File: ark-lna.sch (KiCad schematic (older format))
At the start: 16 parts, among them P1 CONN_1, P2 CONN_1, U1 LM1117-5, U2 MAR-6+

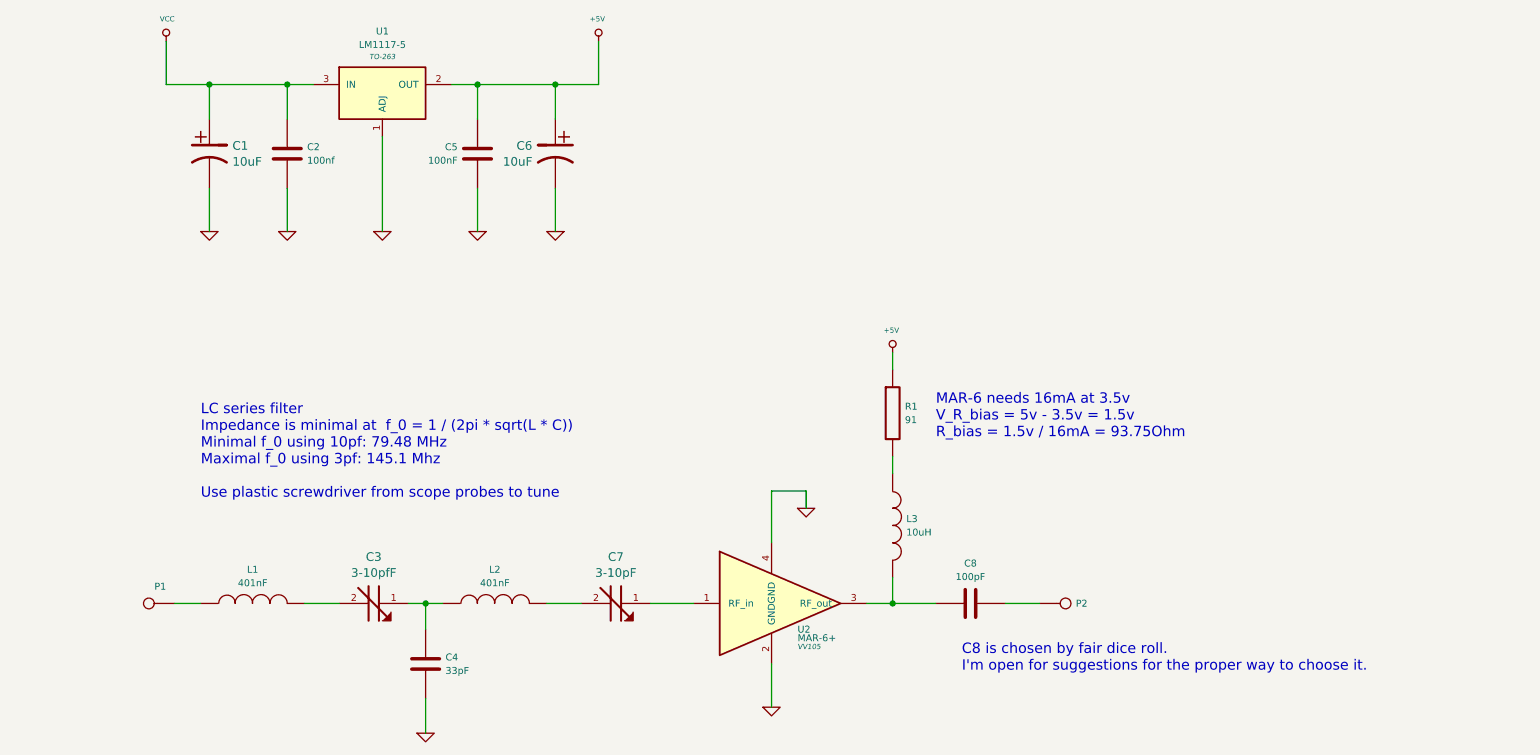
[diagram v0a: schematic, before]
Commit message: Exchanged inductors for better availability Started layouting
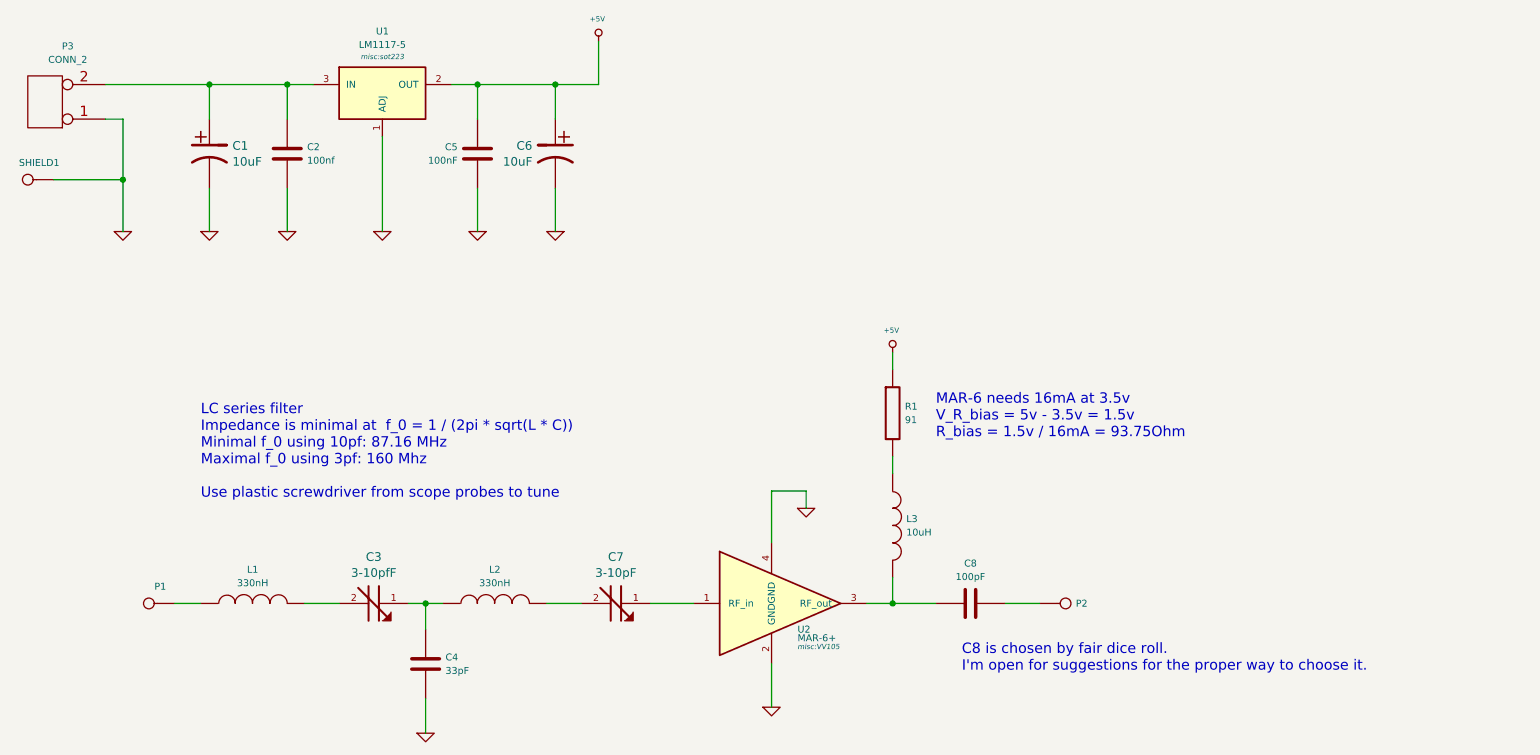
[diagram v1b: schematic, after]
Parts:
- added P3: CONN_2, connect:SIL-2, symbol CONN_2
- added SHIELD1: CONN_1, misc:teko371, symbol CONN_1
- C1, C6: footprint (none) -> smd_capacitors:c_elec_4x5.3
- C2, C5, R1: footprint (none) -> libcms:SM0603
- C3, C7: footprint (none) -> misc:TZC3
- C4, C8, L3: footprint (none) -> libcms:SM0805
- L1, L2: value 401nF -> 330nH; footprint (none) -> libcms:SM0805
- P1, P2: footprint (none) -> connect:1pin
- U1: footprint TO-263 -> misc:sot223
- U2: footprint VV105 -> misc:VV105
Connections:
- net GND: now also P3.1 (P1), SHIELD1.1
- net VCC: no longer names the net of C1.1, C2.1, U1.3 (IN)
- net VCC: now also P3.2 (PM)
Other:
- note added: "LC series filter\nImpedance is minimal at f_0 = 1 / (2pi * sqrt(L * C))\nMinimal f_0 using 10pf: 87.16 MHz\nMaximal f_0 using 3pf: 160 Mhz\n\nUse plastic screwdriver from scope probes to tune"
- note removed: "LC series filter\nImpedance is minimal at f_0 = 1 / (2pi * sqrt(L * C))\nMinimal f_0 using 10pf: 79.48 MHz\nMaximal f_0 using 3pf: 145.1 Mhz\n\nUse plastic screwdriver from scope probes to tune"
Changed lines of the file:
@@
 LIBS:valves
 LIBS:mar-6
+LIBS:ark-lna-cache
 EELAYER 25 0
 EELAYER END
@@
 encoding utf-8
 Sheet 1 1
-Title ""
-Date ""
-Rev ""
-Comp ""
+Title "Ark-LNA"
+Date "2016-06-09"
+Rev "0.1"
+Comp "Abteilung für Angewandte Raumfahrt - Chaos inKL."
 Comment1 ""
 Comment2 ""
@@
 F 0 "P1" H 2984 4452 40  0000 C CNN
 F 1 "CONN_1" H 3050 4605 30  0001 C CNN
-F 2 "" H 3050 4550 60  0000 C CNN
+F 2 "connect:1pin" H 3050 4550 60  0001 C CNN
 F 3 "" H 3050 4550 60  0000 C CNN
 	1    3050 4550
@@
 P 3650 4550
 F 0 "L1" V 3846 4550 40  0000 C CNN
-F 1 "401nF" V 3768 4550 40  0000 C CNN
-F 2 "" H 3650 4550 60  0000 C CNN
+F 1 "330nH" V 3768 4550 40  0000 C CNN
+F 2 "libcms:SM0805" H 3650 4550 60  0001 C CNN
 F 3 "" H 3650 4550 60  0000 C CNN
 	1    3650 4550
@@
 P 5050 4550
 F 0 "L2" V 5246 4550 40  0000 C CNN
-F 1 "401nF" V 5168 4550 40  0000 C CNN
-F 2 "" H 5050 4550 60  0000 C CNN
+F 1 "330nH" V 5168 4550 40  0000 C CNN
+F 2 "libcms:SM0805" H 5050 4550 60  0001 C CNN
 F 3 "" H 5050 4550 60  0000 C CNN
 	1    5050 4550
@@
 F 0 "C3" V 4081 4550 50  0000 C CNN
 F 1 "3-10pfF" V 4173 4550 50  0000 C CNN
-F 2 "" H 4350 4550 60  0000 C CNN
+F 2 "misc:TZC3" H 4350 4550 60  0001 C CNN
 F 3 "" H 4350 4550 60  0000 C CNN
 	1    4350 4550
@@
 F 0 "C7" V 5481 4550 50  0000 C CNN
 F 1 "3-10pF" V 5573 4550 50  0000 C CNN
-F 2 "" H 5750 4550 60  0000 C CNN
+F 2 "misc:TZC3" H 5750 4550 60  0001 C CNN
 F 3 "" H 5750 4550 60  0000 C CNN
 	1    5750 4550
@@
 F 0 "C4" H 4765 4939 40  0000 L CNN
 F 1 "33pF" H 4765 4861 40  0000 L CNN
-F 2 "" H 4688 4750 30  0000 C CNN
+F 2 "libcms:SM0805" H 4688 4750 30  0001 C CNN
 F 3 "" H 4650 4900 60  0000 C CNN
 	1    4650 4900
@@
 	4650 5100 4650 5300
 $Comp
-L GND #PWR5
+L GND #PWR01
 U 1 1 5755E6CD
 P 4650 5300
-F 0 "#PWR5" H 4650 5300 30  0001 C CNN
+F 0 "#PWR01" H 4650 5300 30  0001 C CNN
 F 1 "GND" H 4650 5230 30  0001 C CNN
 F 2 "" H 4650 5300 60  0000 C CNN
@@
 F 0 "U2" H 6800 4400 40  0000 L CNN
 F 1 "MAR-6+" H 6800 4350 40  0000 L CNN
-F 2 "VV105" H 6800 4300 30  0000 L CIN
+F 2 "misc:VV105" H 6800 4300 30  0000 L CIN
 F 3 "" H 6650 4550 60  0000 C CNN
 	1    6650 4550
@@
 	6650 4900 6650 5150
 $Comp
-L GND #PWR10
+L GND #PWR02
 U 1 1 5755E929
 P 6850 4000
-F 0 "#PWR10" H 6850 4000 30  0001 C CNN
+F 0 "#PWR02" H 6850 4000 30  0001 C CNN
 F 1 "GND" H 6850 3930 30  0001 C CNN
 F 2 "" H 6850 4000 60  0000 C CNN
@@
 $EndComp
 $Comp
-L GND #PWR9
+L GND #PWR03
 U 1 1 5755E97C
 P 6650 5150
-F 0 "#PWR9" H 6650 5150 30  0001 C CNN
+F 0 "#PWR03" H 6650 5150 30  0001 C CNN
 F 1 "GND" H 6650 5080 30  0001 C CNN
 F 2 "" H 6650 5150 60  0000 C CNN
@@
 F 0 "L3" H 7429 4139 40  0000 L CNN
 F 1 "10uH" H 7429 4061 40  0000 L CNN
-F 2 "" H 7350 4100 60  0000 C CNN
+F 2 "libcms:SM0805" H 7350 4100 60  0001 C CNN
 F 3 "" H 7350 4100 60  0000 C CNN
 	1    7350 4100
@@
 F 0 "R1" H 7421 3489 40  0000 L CNN
 F 1 "91" H 7421 3411 40  0000 L CNN
-F 2 "" V 7280 3450 30  0000 C CNN
+F 2 "libcms:SM0603" V 7280 3450 30  0001 C CNN
 F 3 "" H 7350 3450 30  0000 C CNN
 	1    7350 3450
@@
 F 0 "P2" H 8409 4550 40  0000 L CNN
 F 1 "CONN_1" H 8350 4605 30  0001 C CNN
-F 2 "" H 8350 4550 60  0000 C CNN
+F 2 "connect:1pin" H 8350 4550 60  0001 C CNN
 F 3 "" H 8350 4550 60  0000 C CNN
 	1    8350 4550
@@
 $EndComp
 $Comp
-L +5V #PWR11
+L +5V #PWR04
 U 1 1 5755ED66
 P 7350 3100
-F 0 "#PWR11" H 7350 3190 20  0001 C CNN
+F 0 "#PWR04" H 7350 3190 20  0001 C CNN
 F 1 "+5V" H 7343 3229 30  0000 C CNN
 F 2 "" H 7350 3100 60  0000 C CNN
@@
 F 0 "C8" V 7568 4550 40  0000 C CNN
 F 1 "100pF" V 7646 4550 40  0000 C CNN
-F 2 "" H 7838 4400 30  0000 C CNN
+F 2 "libcms:SM0805" H 7838 4400 30  0001 C CNN
 F 3 "" H 7800 4550 60  0000 C CNN
 	1    7800 4550
@@
 	8000 4550 8200 4550
 Text Notes 3350 3950 0    60   ~ 0
-LC series filter\nImpedance is minimal at  f_0 = 1 / (2pi * sqrt(L * C))\nMinimal f_0 using 10pf: 79.48 MHz\nMaximal f_0 using 3pf: 145.1 Mhz\n\nUse plastic screwdriver from scope probes to tune
+LC series filter\nImpedance is minimal at  f_0 = 1 / (2pi * sqrt(L * C))\nMinimal f_0 using 10pf: 87.16 MHz\nMaximal f_0 using 3pf: 160 Mhz\n\nUse plastic screwdriver from scope probes to tune
 $Comp
 L LM317S U1
@@
 F 0 "U1" H 4400 1958 40  0000 C CNN
 F 1 "LM1117-5" H 4400 1880 40  0000 C CNN
-F 2 "TO-263" H 4400 1811 30  0000 C CIN
+F 2 "misc:sot223" H 4400 1811 30  0000 C CIN
 F 3 "" H 4400 1600 60  0000 C CNN
 	1    4400 1600
@@
 $EndComp
 $Comp
-L GND #PWR4
+L GND #PWR05
 U 1 1 57560406
 P 4400 2400
-F 0 "#PWR4" H 4400 2400 30  0001 C CNN
+F 0 "#PWR05" H 4400 2400 30  0001 C CNN
 F 1 "GND" H 4400 2330 30  0001 C CNN
 F 2 "" H 4400 2400 60  0000 C CNN
@@
 	1    0    0    -1
 $EndComp
-$Comp
-L VCC #PWR1
-U 1 1 57560432
-P 3150 1300
-F 0 "#PWR1" H 3150 1400 30  0001 C CNN
-F 1 "VCC" H 3156 1429 30  0000 C CNN
-F 2 "" H 3150 1300 60  0000 C CNN
-F 3 "" H 3150 1300 60  0000 C CNN
-	1    3150 1300
-	1    0    0    -1
-$EndComp
-Wire Wire Line
-	3150 1300 3150 1550
-Wire Wire Line
-	3150 1550 4000 1550
+Wire Wire Line
+	2800 1550 4000 1550
 $Comp
 L CP1 C1
@@
 F 0 "C1" H 3533 1996 50  0000 L CNN
 F 1 "10uF" H 3533 1904 50  0000 L CNN
-F 2 "" H 3400 1950 60  0000 C CNN
+F 2 "smd_capacitors:c_elec_4x5.3" H 3400 1950 60  0001 C CNN
 F 3 "" H 3400 1950 60  0000 C CNN
 	1    3400 1950
@@
 F 0 "C2" H 3965 1989 40  0000 L CNN
 F 1 "100nf" H 3965 1911 40  0000 L CNN
-F 2 "" H 3965 1872 30  0000 L CNN
+F 2 "libcms:SM0603" H 3965 1872 30  0001 L CNN
 F 3 "" H 3850 1950 60  0000 C CNN
 	1    3850 1950
@@
 	4400 2400 4400 1850
 $Comp
-L GND #PWR3
+L GND #PWR06
 U 1 1 57560722
 P 3850 2400
-F 0 "#PWR3" H 3850 2400 30  0001 C CNN
+F 0 "#PWR06" H 3850 2400 30  0001 C CNN
 F 1 "GND" H 3850 2330 30  0001 C CNN
 F 2 "" H 3850 2400 60  0000 C CNN
@@
 $EndComp
 $Comp
-L GND #PWR2
+L GND #PWR07
 U 1 1 57560752
 P 3400 2400
-F 0 "#PWR2" H 3400 2400 30  0001 C CNN
+F 0 "#PWR07" H 3400 2400 30  0001 C CNN
 F 1 "GND" H 3400 2330 30  0001 C CNN
 F 2 "" H 3400 2400 60  0000 C CNN
@@
 F 0 "C6" H 5533 1996 50  0000 L CNN
 F 1 "10uF" H 5533 1904 50  0000 L CNN
-F 2 "" H 5400 1950 60  0000 C CNN
+F 2 "smd_capacitors:c_elec_4x5.3" H 5400 1950 60  0001 C CNN
 F 3 "" H 5400 1950 60  0000 C CNN
 	1    5400 1950
@@
 F 0 "C5" H 5065 1989 40  0000 L CNN
 F 1 "100nF" H 5065 1911 40  0000 L CNN
-F 2 "" H 4988 1800 30  0000 C CNN
+F 2 "libcms:SM0603" H 4988 1800 30  0001 C CNN
 F 3 "" H 4950 1950 60  0000 C CNN
 	1    4950 1950
@@
 	4950 2400 4950 2150
 $Comp
-L GND #PWR6
+L GND #PWR08
 U 1 1 57560990
 P 4950 2400
-F 0 "#PWR6" H 4950 2400 30  0001 C CNN
+F 0 "#PWR08" H 4950 2400 30  0001 C CNN
 F 1 "GND" H 4950 2330 30  0001 C CNN
 F 2 "" H 4950 2400 60  0000 C CNN
@@
 $EndComp
 $Comp
-L GND #PWR7
+L GND #PWR09
 U 1 1 57560996
 P 5400 2400
-F 0 "#PWR7" H 5400 2400 30  0001 C CNN
+F 0 "#PWR09" H 5400 2400 30  0001 C CNN
 F 1 "GND" H 5400 2330 30  0001 C CNN
 F 2 "" H 5400 2400 60  0000 C CNN
@@
 	5650 1550 5650 1300
 $Comp
-L +5V #PWR8
+L +5V #PWR010
 U 1 1 57560C9E
 P 5650 1300
-F 0 "#PWR8" H 5650 1390 20  0001 C CNN
+F 0 "#PWR010" H 5650 1390 20  0001 C CNN
 F 1 "+5V" H 5643 1429 30  0000 C CNN
 F 2 "" H 5650 1300 60  0000 C CNN
@@
 Text Notes 7750 4950 0    60   ~ 0
 C8 is chosen by fair dice roll.\nI'm open for suggestions for the proper way to choose it.
+$Comp
+L CONN_2 P3
+U 1 1 57589A35
+P 2450 1650
+F 0 "P3" H 2319 1328 40  0000 C CNN
+F 1 "CONN_2" H 2319 1406 40  0000 C CNN
+F 2 "connect:SIL-2" H 2450 1650 60  0001 C CNN
+F 3 "" H 2450 1650 60  0000 C CNN
+	1    2450 1650
+	-1   0    0    1
+$EndComp
+Wire Wire Line
+	2800 1750 2900 1750
+Wire Wire Line
+	2900 1750 2900 2400
+$Comp
+L GND #PWR011
+U 1 1 57589C33
+P 2900 2400
+F 0 "#PWR011" H 2900 2400 30  0001 C CNN
+F 1 "GND" H 2900 2330 30  0001 C CNN
+F 2 "" H 2900 2400 60  0000 C CNN
+F 3 "" H 2900 2400 60  0000 C CNN
+	1    2900 2400
+	1    0    0    -1
+$EndComp
+$Comp
+L CONN_1 SHIELD1
+U 1 1 57589F67
+P 2350 2100
+F 0 "SHIELD1" H 2284 2002 40  0000 C CNN
+F 1 "CONN_1" H 2350 2155 30  0001 C CNN
+F 2 "misc:teko371" H 2350 2100 60  0001 C CNN
+F 3 "" H 2350 2100 60  0000 C CNN
+	1    2350 2100
+	-1   0    0    1
+$EndComp
+Wire Wire Line
+	2500 2100 2900 2100
+Connection ~ 2900 2100
 $EndSCHEMATC
